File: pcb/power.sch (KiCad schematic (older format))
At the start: 14 parts

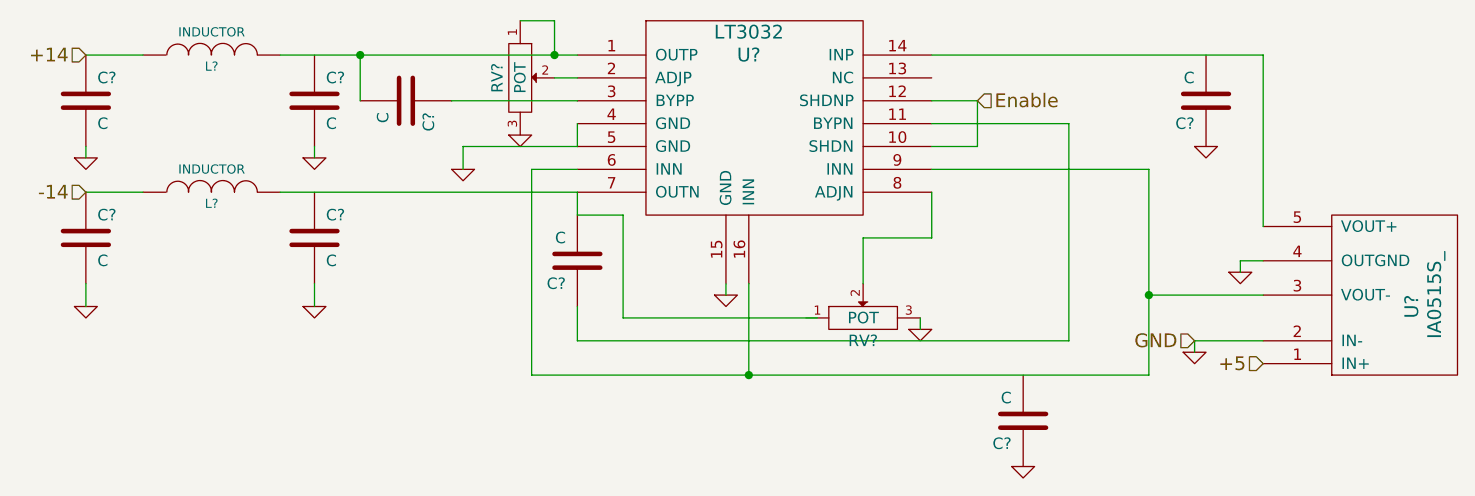
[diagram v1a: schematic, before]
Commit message: fixed all pcb components
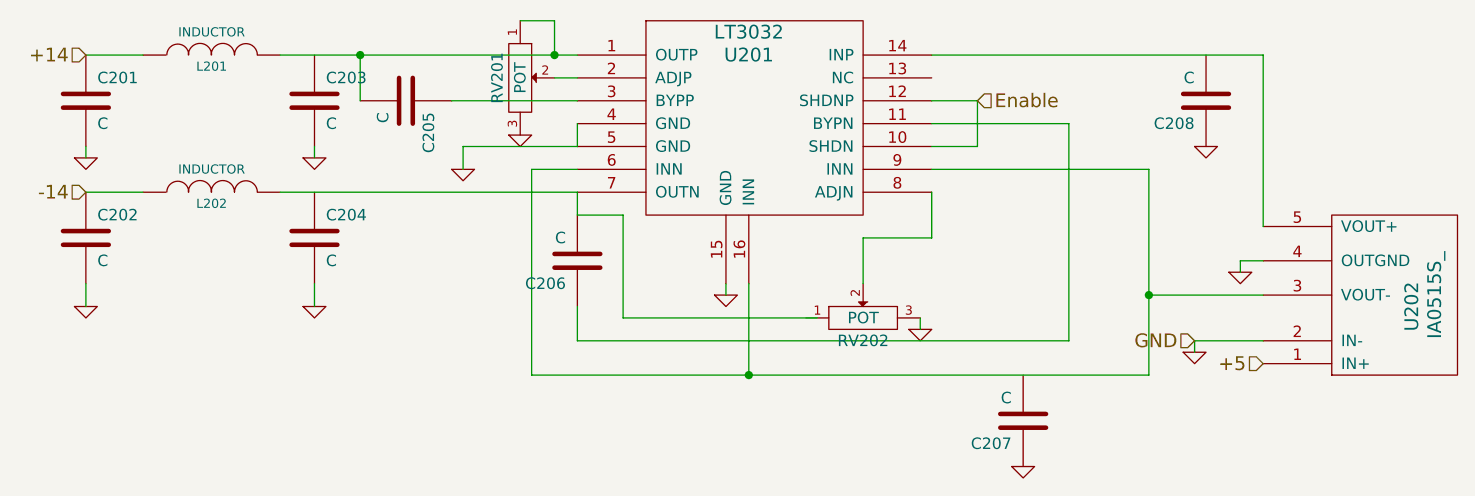
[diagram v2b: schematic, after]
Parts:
- gave numbers to parts that had none: 14
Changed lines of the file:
@@
-EESchema Schematic File Version 2  date Wed 27 Mar 2013 08:49:56 PM CET
+EESchema Schematic File Version 2  date Thu 28 Mar 2013 07:13:51 PM CET
 LIBS:power
 LIBS:device
@@
 Sheet 2 6
 Title ""
-Date "27 mar 2013"
+Date "28 mar 2013"
 Rev ""
 Comp ""
@@
 $EndDescr
 $Comp
-L IA0515S_ U?
+L IA0515S_ U202
 U 1 1 5151B8BD
 P 8700 4050
-F 0 "U?" H 8450 4050 60  0000 C CNN
+F 0 "U202" H 8450 4050 60  0000 C CNN
 F 1 "IA0515S_" H 8500 4150 60  0000 C CNN
 	1    8700 4050
@@
 $EndComp
 $Comp
-L LT3032 U?
+L LT3032 U201
 U 1 1 5151B8CC
 P 5800 3450
-F 0 "U?" H 5800 3700 60  0000 C CNN
+F 0 "U201" H 5800 3700 60  0000 C CNN
 F 1 "LT3032" H 5800 3800 60  0000 C CNN
 	1    5800 3450
@@
 $EndComp
 $Comp
-L C C?
+L C C205
 U 1 1 5151BA9D
 P 4300 3400
-F 0 "C?" H 4350 3500 50  0000 L CNN
+F 0 "C205" H 4350 3500 50  0000 L CNN
 F 1 "C" H 4350 3300 50  0000 L CNN
 	1    4300 3400
@@
 $EndComp
 $Comp
-L C C?
+L C C206
 U 1 1 5151BAAC
 P 5050 4100
-F 0 "C?" H 5100 4200 50  0000 L CNN
+F 0 "C206" H 5100 4200 50  0000 L CNN
 F 1 "C" H 5100 4000 50  0000 L CNN
 	1    5050 4100
@@
 $EndComp
 $Comp
-L POT RV?
+L POT RV202
 U 1 1 5151EBB9
 P 6300 4350
-F 0 "RV?" H 6300 4250 50  0000 C CNN
+F 0 "RV202" H 6300 4250 50  0000 C CNN
 F 1 "POT" H 6300 4350 50  0000 C CNN
 	1    6300 4350
@@
 $EndComp
 $Comp
-L GND #PWR?
+L GND #PWR019
 U 1 1 5151EC02
 P 6550 4400
-F 0 "#PWR?" H 6550 4400 30  0001 C CNN
+F 0 "#PWR019" H 6550 4400 30  0001 C CNN
 F 1 "GND" H 6550 4330 30  0001 C CNN
 	1    6550 4400
@@
 $EndComp
 $Comp
-L GND #PWR?
+L GND #PWR020
 U 1 1 5151EC1E
 P 5700 4250
-F 0 "#PWR?" H 5700 4250 30  0001 C CNN
+F 0 "#PWR020" H 5700 4250 30  0001 C CNN
 F 1 "GND" H 5700 4180 30  0001 C CNN
 	1    5700 4250
@@
 $EndComp
 $Comp
-L POT RV?
+L POT RV201
 U 1 1 5151EC34
 P 4800 3300
-F 0 "RV?" H 4800 3200 50  0000 C CNN
+F 0 "RV201" H 4800 3200 50  0000 C CNN
 F 1 "POT" H 4800 3300 50  0000 C CNN
 	1    4800 3300
@@
 $EndComp
 $Comp
-L GND #PWR?
+L GND #PWR021
 U 1 1 5151EC5D
 P 4800 3550
-F 0 "#PWR?" H 4800 3550 30  0001 C CNN
+F 0 "#PWR021" H 4800 3550 30  0001 C CNN
 F 1 "GND" H 4800 3480 30  0001 C CNN
 	1    4800 3550
@@
 Connection ~ 5800 4600
 $Comp
-L GND #PWR?
+L GND #PWR022
 U 1 1 5151ED14
 P 7950 4150
-F 0 "#PWR?" H 7950 4150 30  0001 C CNN
+F 0 "#PWR022" H 7950 4150 30  0001 C CNN
 F 1 "GND" H 7950 4080 30  0001 C CNN
 	1    7950 4150
@@
 	7950 4100 7950 4150
 $Comp
-L INDUCTOR L?
+L INDUCTOR L201
 U 1 1 5151ED3F
 P 3450 3200
-F 0 "L?" V 3400 3200 40  0000 C CNN
+F 0 "L201" V 3400 3200 40  0000 C CNN
 F 1 "INDUCTOR" V 3550 3200 40  0000 C CNN
 	1    3450 3200
@@
 $EndComp
 $Comp
-L INDUCTOR L?
+L INDUCTOR L202
 U 1 1 5151ED82
 P 3450 3800
-F 0 "L?" V 3400 3800 40  0000 C CNN
+F 0 "L202" V 3400 3800 40  0000 C CNN
 F 1 "INDUCTOR" V 3550 3800 40  0000 C CNN
 	1    3450 3800
@@
 Connection ~ 4100 3200
 $Comp
-L C C?
+L C C201
 U 1 1 5151EE2F
 P 2900 3400
-F 0 "C?" H 2950 3500 50  0000 L CNN
+F 0 "C201" H 2950 3500 50  0000 L CNN
 F 1 "C" H 2950 3300 50  0000 L CNN
 	1    2900 3400
@@
 $EndComp
 $Comp
-L C C?
+L C C202
 U 1 1 5151EE35
 P 2900 4000
-F 0 "C?" H 2950 4100 50  0000 L CNN
+F 0 "C202" H 2950 4100 50  0000 L CNN
 F 1 "C" H 2950 3900 50  0000 L CNN
 	1    2900 4000
@@
 $EndComp
 $Comp
-L GND #PWR?
+L GND #PWR023
 U 1 1 5151EE3B
 P 2900 3650
-F 0 "#PWR?" H 2900 3650 30  0001 C CNN
+F 0 "#PWR023" H 2900 3650 30  0001 C CNN
 F 1 "GND" H 2900 3580 30  0001 C CNN
 	1    2900 3650
@@
 $EndComp
 $Comp
-L GND #PWR?
+L GND #PWR024
 U 1 1 5151EE41
 P 2900 4300
-F 0 "#PWR?" H 2900 4300 30  0001 C CNN
+F 0 "#PWR024" H 2900 4300 30  0001 C CNN
 F 1 "GND" H 2900 4230 30  0001 C CNN
 	1    2900 4300
@@
 	2900 4200 2900 4300
 $Comp
-L C C?
+L C C208
 U 1 1 5151EEE9
 P 7800 3400
-F 0 "C?" H 7850 3500 50  0000 L CNN
+F 0 "C208" H 7850 3500 50  0000 L CNN
 F 1 "C" H 7850 3300 50  0000 L CNN
 	1    7800 3400
@@
 $EndComp
 $Comp
-L C C?
+L C C207
 U 1 1 5151EEEF
 P 7000 4800
-F 0 "C?" H 7050 4900 50  0000 L CNN
+F 0 "C207" H 7050 4900 50  0000 L CNN
 F 1 "C" H 7050 4700 50  0000 L CNN
 	1    7000 4800
@@
 $EndComp
 $Comp
-L GND #PWR?
+L GND #PWR025
 U 1 1 5151EEF5
 P 7000 5000
-F 0 "#PWR?" H 7000 5000 30  0001 C CNN
+F 0 "#PWR025" H 7000 5000 30  0001 C CNN
 F 1 "GND" H 7000 4930 30  0001 C CNN
 	1    7000 5000
@@
 $EndComp
 $Comp
-L GND #PWR?
+L GND #PWR026
 U 1 1 5151EEFB
 P 7800 3600
-F 0 "#PWR?" H 7800 3600 30  0001 C CNN
+F 0 "#PWR026" H 7800 3600 30  0001 C CNN
 F 1 "GND" H 7800 3530 30  0001 C CNN
 	1    7800 3600
@@
 $EndComp
 $Comp
-L GND #PWR?
+L GND #PWR027
 U 1 1 5151EF2F
 P 4550 3700
-F 0 "#PWR?" H 4550 3700 30  0001 C CNN
+F 0 "#PWR027" H 4550 3700 30  0001 C CNN
 F 1 "GND" H 4550 3630 30  0001 C CNN
 	1    4550 3700
@@
 -14
 $Comp
-L GND #PWR?
+L GND #PWR028
 U 1 1 5151EF8D
 P 7750 4500
-F 0 "#PWR?" H 7750 4500 30  0001 C CNN
+F 0 "#PWR028" H 7750 4500 30  0001 C CNN
 F 1 "GND" H 7750 4430 30  0001 C CNN
 	1    7750 4500
@@
 GND
 $Comp
-L C C?
+L C C203
 U 1 1 5151F0BF
 P 3900 3400
-F 0 "C?" H 3950 3500 50  0000 L CNN
+F 0 "C203" H 3950 3500 50  0000 L CNN
 F 1 "C" H 3950 3300 50  0000 L CNN
 	1    3900 3400
@@
 $EndComp
 $Comp
-L C C?
+L C C204
 U 1 1 5151F0C5
 P 3900 4000
-F 0 "C?" H 3950 4100 50  0000 L CNN
+F 0 "C204" H 3950 4100 50  0000 L CNN
 F 1 "C" H 3950 3900 50  0000 L CNN
 	1    3900 4000
@@
 $EndComp
 $Comp
-L GND #PWR?
+L GND #PWR029
 U 1 1 5151F0CB
 P 3900 3650
-F 0 "#PWR?" H 3900 3650 30  0001 C CNN
+F 0 "#PWR029" H 3900 3650 30  0001 C CNN
 F 1 "GND" H 3900 3580 30  0001 C CNN
 	1    3900 3650
@@
 $EndComp
 $Comp
-L GND #PWR?
+L GND #PWR030
 U 1 1 5151F0D1
 P 3900 4300
-F 0 "#PWR?" H 3900 4300 30  0001 C CNN
+F 0 "#PWR030" H 3900 4300 30  0001 C CNN
 F 1 "GND" H 3900 4230 30  0001 C CNN
 	1    3900 4300
